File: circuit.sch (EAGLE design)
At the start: 12 parts, among them IC1 MEGA8-P

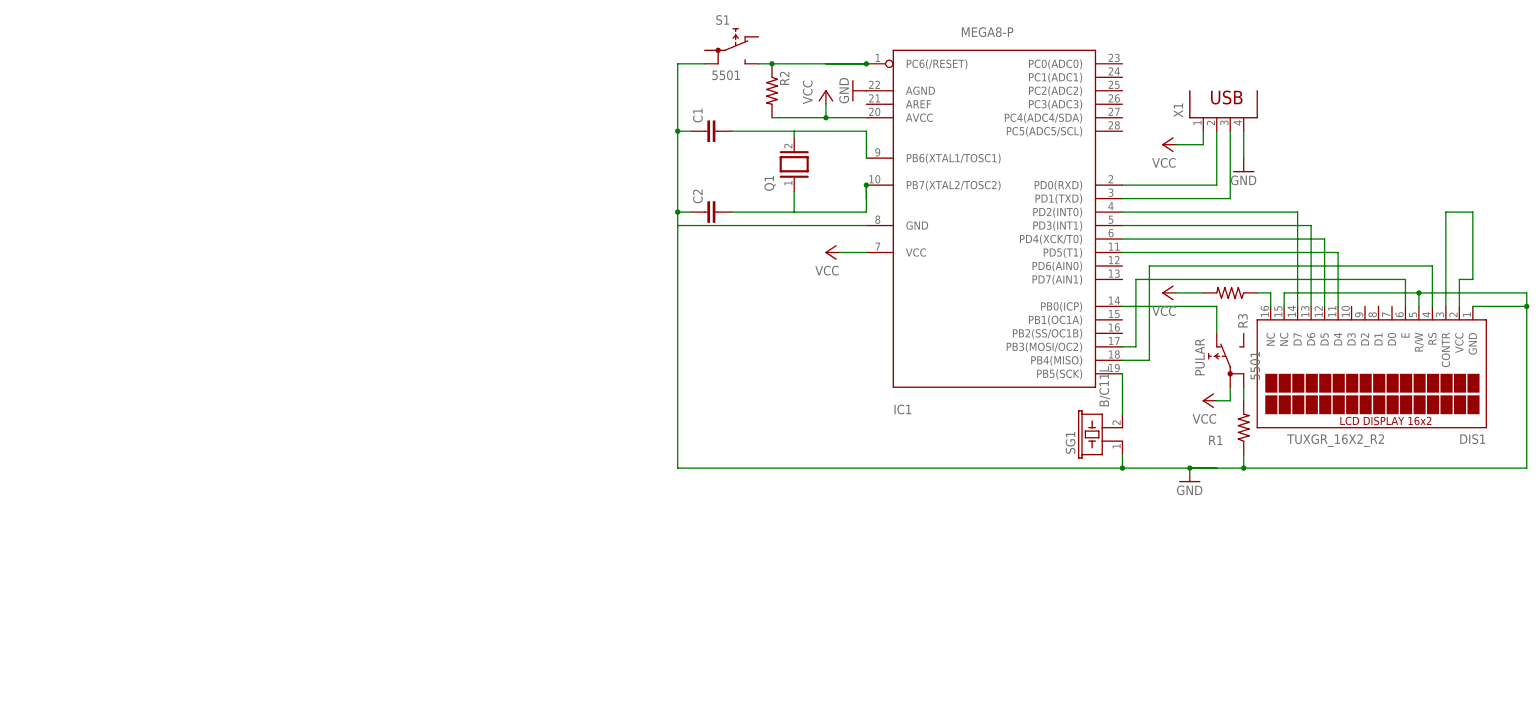
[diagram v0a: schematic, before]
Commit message: Atualização das trilhas com os modelos 3D
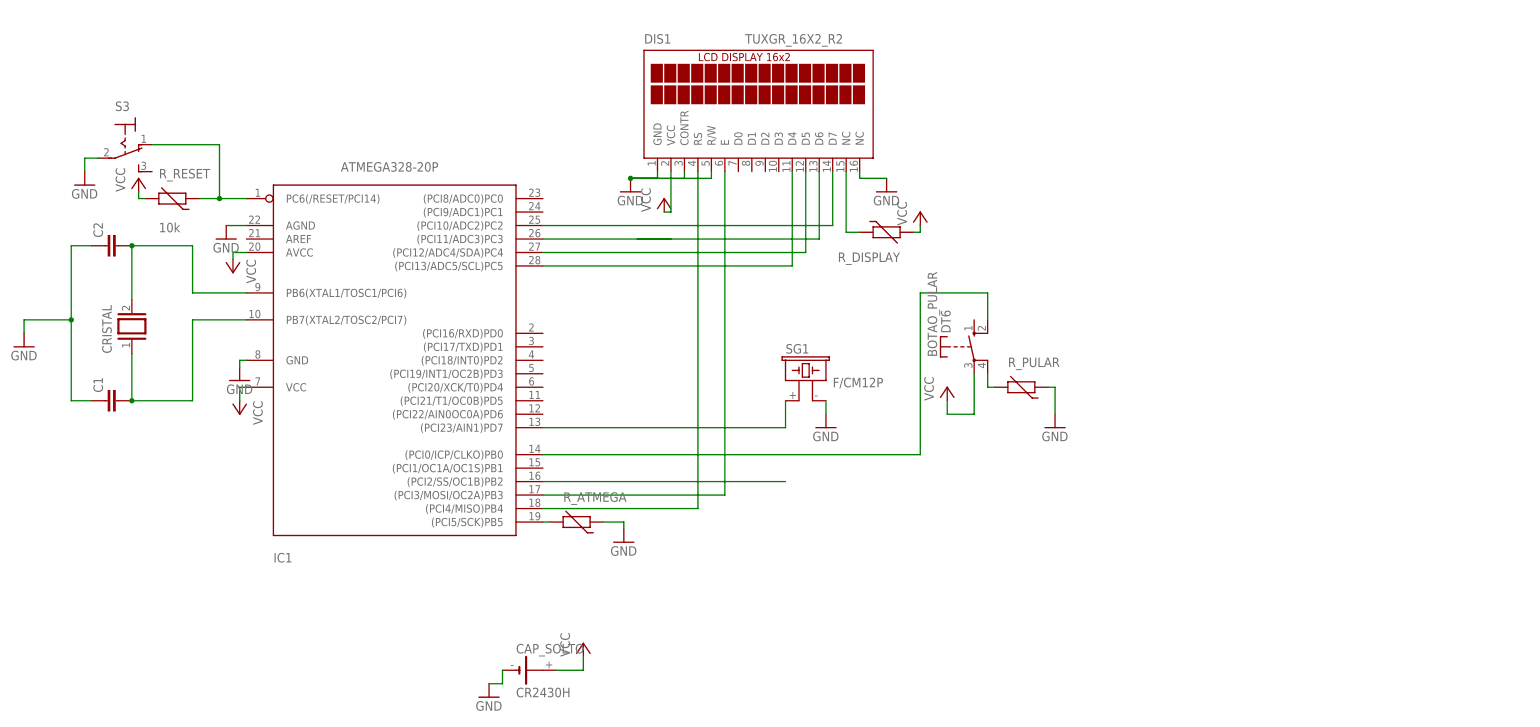
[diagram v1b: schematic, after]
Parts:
- removed PULAR, S1: 5501, switch:5501
- removed Q1: (no value), special:XTAL/S
- removed R1, R2, R3: (no value), rcl:R-US_0204/5
- removed X1: (no value), con-berg:PN87520
- added BOTAO_PULAR: DT6, switch-misc:DT6
- added CAP_SOLTO: CR2430H, battery:CR2430H
- added CRISTAL: (no value), special:XTAL/S
- added R_ATMEGA, R_DISPLAY, R_PULAR: (no value), discrete:THERMISTOR_R-5
- added R_RESET: 10k, discrete:THERMISTOR_R-5
- added S3: (no value), switch:320-916
- C1, C2: device capacitor-wima:C2.5/4 -> capacitor-wima:C2.5/2
- IC1: value MEGA8-P -> ATMEGA328-20P; device avr-7:MEGA8-P -> atmega328:ATMEGA328-20P
- SG1: value B/C11L -> F/CM12P; device buzzer:B/C11L -> buzzer:F/CM12P
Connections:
- removed net N$14: DIS1.NC@2, R3.1
- removed net N$2: DIS1.D6, IC1.PD3(INT1)
- removed net N$3: C2.2, IC1.PB7(XTAL2/TOSC2), Q1.1
- new net N$19: BOTAO_PULAR.S@1, IC1.(PCI0/ICP/CLKO)PB0
- new net N$8: DIS1.NC@1, R_DISPLAY.1
- net GND: now also CAP_SOLTO.-, DIS1.CONTR, DIS1.NC@2, IC1.GND, R_ATMEGA.1, R_PULAR.1, S3.P, SG1.2; no longer DIS1.NC@1, IC1.GND@1, R1.1, S1.1B, SG1.1, X1.4
- net N$1: now also IC1.(PCI23/AIN1)PD7, SG1.1; no longer DIS1.D7, IC1.PD2(INT0)
- net N$10: now also DIS1.E, IC1.(PCI3/MOSI/OC2A)PB3; no longer DIS1.D4, IC1.PD5(T1)
- net N$11: now also DIS1.D4, IC1.(PCI13/ADC5/SCL)PC5; no longer DIS1.RS, IC1.PB4(MISO)
- net N$12: now also DIS1.D5, IC1.(PCI12/ADC4/SDA)PC4; no longer IC1.PB5(SCK), SG1.2
- net N$13: now also DIS1.D6, IC1.(PCI11/ADC3)PC3; no longer DIS1.E, IC1.PB3(MOSI/OC2)
- net N$15: now also DIS1.D7, IC1.(PCI10/ADC2)PC2; no longer DIS1.CONTR, DIS1.VCC
- net N$16: now also IC1.(PCI2/SS/OC1B)PB2; no longer IC1.PD0(RXD), X1.2
- net N$17: now also BOTAO_PULAR.P@1, R_PULAR.2; no longer IC1.PD1(TXD), X1.3
- net N$4: now also IC1.PC6(/RESET/PCI14), R_RESET.1, S3.O; no longer C1.2, IC1.PB6(XTAL1/TOSC1), Q1.2
- net N$5: now also C1.2, CRISTAL.1, IC1.PB7(XTAL2/TOSC2/PCI7); no longer DIS1.D5, IC1.PD4(XCK/T0)
- net N$6: now also C2.2, CRISTAL.2, IC1.PB6(XTAL1/TOSC1/PCI6); no longer PULAR.1B, R1.2
- net N$7: now also IC1.(PCI5/SCK)PB5, R_ATMEGA.2; no longer IC1.PB0(ICP), PULAR.NC
- net N$9: now also DIS1.RS, IC1.(PCI4/MISO)PB4; no longer IC1.PC6(/RESET), R2.1, S1.NO
- net VCC: now also BOTAO_PULAR.P, CAP_SOLTO.+, DIS1.VCC, IC1.VCC, R_DISPLAY.2, R_RESET.2; no longer IC1.VCC@1, PULAR.1A, R2.2, R3.2, X1.1
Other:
- moved on the sheet: C1, C2, DIS1, IC1, SG1

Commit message: Versão final do circuito
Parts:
- removed CAP_SOLTO: CR2430H, battery:CR2430H
- removed R_ATMEGA, R_DISPLAY, R_PULAR: (no value), discrete:THERMISTOR_R-5
- removed R_RESET: 10k, discrete:THERMISTOR_R-5
- added G1: CR2032H, battery:CR2032H
- added R1, R2, R3, R4: (no value), rcl:R-US_0204/7
- C1, C2: device capacitor-wima:C2.5/2 -> capacitor-wima:C5/3.5
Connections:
- removed net N$7: IC1.(PCI5/SCK)PB5, R_ATMEGA.2
- removed net N$8: DIS1.NC@1, R_DISPLAY.1
- new net N$2: IC1.(PCI5/SCK)PB5, R2.1
- new net N$3: DIS1.NC@1, R3.1
- net GND: now also G1.-, R1.2, R2.2; no longer CAP_SOLTO.-, R_ATMEGA.1, R_PULAR.1
- net N$17: now also R1.1; no longer R_PULAR.2
- net N$4: now also R4.2; no longer R_RESET.1
- net VCC: now also G1.+, R3.2, R4.1; no longer CAP_SOLTO.+, R_DISPLAY.2, R_RESET.2
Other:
- moved on the sheet: C1, C2
